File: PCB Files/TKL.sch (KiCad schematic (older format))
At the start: 632 parts, among them J1 USB_C, SW1 ESC, SW10 F9, SW100 RGUI_R2, SW101 RCTRL_R2, SW102 STEPPED_CAPS, SW103 RSHFT_175, SW104 Fn, SW105 BKSP_2U, SW11 F10, SW12 F11, SW13 F12, SW14 PRTSC, SW15 SCRLCK, SW16 PAUSE, SW17 GRV, SW18 1, SW19 2, SW2 F1, SW20 3, SW21 4, SW22 5, SW23 6, SW24 7, SW25 8, SW26 9, SW27 0, SW28 HIFEN, SW29 PLUS, SW3 F2, SW30 BCKSLSH, SW31 DEL, SW32 INS, SW33 HOME, SW34 PGUP, SW35 TAB, SW36 Q, SW37 W, SW38 E, SW39 R, SW4 F3, SW40 T, SW41 Y, SW42 U, SW43 I, SW44 O, SW45 P, SW46 LBRACES, SW47 RBRACES, SW48 BKSP_150, SW49 DEL, SW5 F4, SW50 END, SW51 PGDN, SW52 CAPS, SW53 A, SW54 S, SW55 D, SW56 F, SW57 G, SW58 H, SW59 J, SW6 F5, SW60 K, SW61 L, SW62 :, SW63 QUOTE, SW64 ENTER, SW65 LSHFT, SW66 Z, SW67 X, SW68 C, SW69 V, SW7 F6, SW70 B, SW71 N, SW72 M, SW73 <,, SW74 .>, SW75 /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

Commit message: Routed RGB76
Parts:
- added D96: 1N4148, acheron_Components:D_SOD-123, symbol Device:D
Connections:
- net Col1: now also U200.27 (ADC10/T0/PD7); no longer U200.40 (ADC1/PF1)
- net Col16: now also U200.25 (ADC8/PD4); no longer U200.27 (ADC10/T0/PD7)
- net Col17: now also U200.22 (PD5/~CTS~/XCK1); no longer U200.26 (ADC9/T1/PD6)
- net Col18: now also U200.21 (PD3/TXD1/~INT3~); no longer U200.25 (ADC8/PD4)
- net Col7: now also U200.40 (ADC1/PF1); no longer U200.36 (ADC7/PF7)
- net Col8: now also U200.36 (ADC7/PF7)
- net L4: no longer SW96.2 (Row)
- net RGB_DIN: now also U200.26 (ADC9/T1/PD6)
- net Row6: now also D96.1 (K)
- net at U75.5 (DO): now also RD103.2; no longer RD76.2
- net at U76.5 (DO): now also RD104.2; no longer RD103.2
- net at U103.5 (DO): now also RD76.2; no longer RD104.2
- new net: D96.2 (A), SW96.2 (Row)
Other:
- moved on the sheet: C103, C76, L103, L76, R103, R76, RD103, RD76, U103, U76

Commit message: Added last row RGB components to schematic
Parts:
- added C? (x14): 100nF, Capacitor_SMD:C_0805_2012Metric, symbol Device:C_Small
- added D93: 1N4148, acheron_Components:D_SOD-123, symbol Device:D
- added L? (x14): LED_BGRA, acheron_Components:LED_RGB_SMD_6028_2.8x3.5mm_Round, symbol Device:LED_BGRA
- added R? (x14): 100R, Resistor_SMD:R_0805_2012Metric, symbol Device:R_Small
- added RD? (x14): 33R, Resistor_SMD:R_0805_2012Metric, symbol Device:R_Small
- added U? (x14): WS2811M, acheron_Components:MSOP-8-1EP_3x3mm_P0.65mm_EP1.68x1.88mm, symbol acheronSymbols:WS2811M
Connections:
- net 5V: now also L?.4 (A), L?.4 (A), L?.4 (A), L?.4 (A), L?.4 (A), L?.4 (A), L?.4 (A), L?.4 (A), L?.4 (A), L?.4 (A), L?.4 (A), L?.4 (A), L?.4 (A), L?.4 (A), R?.1, R?.1, R?.1, R?.1, R?.1, R?.1, R?.1, R?.1, R?.1, R?.1, R?.1, R?.1, R?.1, R?.1
- net GND: now also C?.2, C?.2, C?.2, C?.2, C?.2, C?.2, C?.2, C?.2, C?.2, C?.2, C?.2, C?.2, C?.2, C?.2, U?.4 (GND), U?.4 (GND), U?.4 (GND), U?.4 (GND), U?.4 (GND), U?.4 (GND), U?.4 (GND), U?.4 (GND), U?.4 (GND), U?.4 (GND), U?.4 (GND), U?.4 (GND), U?.4 (GND), U?.4 (GND), U?.9 (GND), U?.9 (GND), U?.9 (GND), U?.9 (GND), U?.9 (GND), U?.9 (GND), U?.9 (GND), U?.9 (GND), U?.9 (GND), U?.9 (GND), U?.9 (GND), U?.9 (GND), U?.9 (GND), U?.9 (GND)
- net L3: no longer SW93.2 (Row)
- net Row5: now also D73.1 (K)
- net Row6: now also D93.1 (K)
- net at U77.5 (DO): now also RD?.2
- new net: D93.2 (A), SW93.2 (Row)
- new net: L?.3 (RK), U?.1 (OUTR) (x14)
- new net: L?.2 (GK), U?.2 (OUTG) (x14)
- new net: L?.1 (BK), U?.3 (OUTB) (x14)
- new net: RD?.2, U?.5 (DO) (x12)
- new net: RD?.1, U?.6 (DIN) (x13)
- new net: C?.1, R?.2, U?.8 (VDD) (x14)
- new net: RD?.1, U?.5 (DO)
- new net: RD?.2, U?.6 (DIN)
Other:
- moved on the sheet: D73, SW73

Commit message: Routed SW88 RGB LED
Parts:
- removed C? (x3): 100nF, Capacitor_SMD:C_0805_2012Metric, symbol Device:C_Small
- removed L? (x3): LED_BGRA, acheron_Components:LED_RGB_SMD_6028_2.8x3.5mm_Round, symbol Device:LED_BGRA
- removed R? (x3): 100R, Resistor_SMD:R_0805_2012Metric, symbol Device:R_Small
- removed RD? (x3): 33R, Resistor_SMD:R_0805_2012Metric, symbol Device:R_Small
- removed U? (x3): WS2811M, acheron_Components:MSOP-8-1EP_3x3mm_P0.65mm_EP1.68x1.88mm, symbol acheronSymbols:WS2811M
- gave numbers to parts that had none: 55
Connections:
- net at U77.5 (DO): now also RD88.2
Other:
- moved on the sheet: C78, C79, C80, C81, C82, C83, C84, C85, C86, C87, C88, L78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

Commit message: Placed last row LEDs
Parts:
- added C97, C99: 100nF, Capacitor_SMD:C_0805_2012Metric, symbol Device:C_Small
- added L91, L93, L94, L95, L96, L97, L99: LED_BGRA, acheron_Components:LED_RGB_SMD_6028_2.8x3.5mm_Round, symbol Device:LED_BGRA
- added R97, R99: 100R, Resistor_SMD:R_0805_2012Metric, symbol Device:R_Small
- added RD97, RD99: 33R, Resistor_SMD:R_0805_2012Metric, symbol Device:R_Small
- added U97, U99: WS2811M, acheron_Components:MSOP-8-1EP_3x3mm_P0.65mm_EP1.68x1.88mm, symbol acheronSymbols:WS2811M
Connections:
- net 5V: now also L97.4 (A), L99.4 (A), R97.1, R99.1
- net GND: now also C97.2, C99.2, U97.4 (GND), U97.9 (GND), U99.4 (GND), U99.9 (GND)
- net at RD82.2: now also U97.5 (DO); no longer U83.5 (DO)
- net at RD83.2: now also U99.5 (DO); no longer U84.5 (DO)
- new net: RD99.2, U84.5 (DO)
- new net: RD99.1, U99.6 (DIN)
- new net: L99.3 (RK), U99.1 (OUTR)
- new net: L99.2 (GK), U99.2 (OUTG)
- new net: L99.1 (BK), U99.3 (OUTB)
- new net: C99.1, R99.2, U99.8 (VDD)
- new net: RD97.1, U97.6 (DIN)
- new net: L97.3 (RK), U97.1 (OUTR)
- new net: L97.2 (GK), U97.2 (OUTG)
- new net: L97.1 (BK), U97.3 (OUTB)
- new net: C97.1, R97.2, U97.8 (VDD)
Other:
- moved on the sheet: C78, C79, C80, C81, C82, C83, C84, L78, L79, L80, L81, L82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

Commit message: Update: routed more RGBs, removed split bottom row
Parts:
- removed C97, C99: 100nF, Capacitor_SMD:C_0805_2012Metric, symbol Device:C_Small
- removed D89, D96: 1N4148, acheron_Components:D_SOD-123, symbol Device:D
- removed L91, L94, L96, L97, L99: LED_BGRA, acheron_Components:LED_RGB_SMD_6028_2.8x3.5mm_Round, symbol Device:LED_BGRA
- removed R97, R99: 100R, Resistor_SMD:R_0805_2012Metric, symbol Device:R_Small
- removed RD97, RD99: 33R, Resistor_SMD:R_0805_2012Metric, symbol Device:R_Small
- removed SW91: LALT_B3, acheron_MX:MX100, symbol acheronSymbols:MXSwitch
- removed SW94: LSPC_R3, acheron_MX:MX225R, symbol acheronSymbols:MXSwitch
- removed SW96: RSPC_B3, acheron_MX:MX275R, symbol acheronSymbols:MXSwitch
- removed SW97: RGUI_R3, acheron_MX:MX125, symbol acheronSymbols:MXSwitch
- removed SW99: RALT_R3, acheron_MX:MX100, symbol acheronSymbols:MXSwitch
- removed U97, U99: WS2811M, acheron_Components:MSOP-8-1EP_3x3mm_P0.65mm_EP1.68x1.88mm, symbol acheronSymbols:WS2811M
- added C95: 100nF, Capacitor_SMD:C_0805_2012Metric, symbol Device:C_Small
- added R95: 100R, Resistor_SMD:R_0805_2012Metric, symbol Device:R_Small
- added RD95: 33R, Resistor_SMD:R_0805_2012Metric, symbol Device:R_Small
- added U95: WS2811M, acheron_Components:MSOP-8-1EP_3x3mm_P0.65mm_EP1.68x1.88mm, symbol acheronSymbols:WS2811M
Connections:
- net 5V: now also L95.4 (A), R95.1
- net GND: now also C95.2, U95.4 (GND), U95.9 (GND)
- net at RD82.2: now also U95.5 (DO)
- net at RD83.2: now also U84.5 (DO)
- net at U83.5 (DO): now also RD95.2
- net at L95.1 (BK): now also U95.3 (OUTB)
- net at L95.2 (GK): now also U95.2 (OUTG)
- net at L95.3 (RK): now also U95.1 (OUTR)
- new net: RD95.1, U95.6 (DIN)
- new net: C95.1, R95.2, U95.8 (VDD)
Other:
- moved on the sheet: L95

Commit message: Update: Finish routing
- All tracks were routed

- There are some extra pins that need to be broken out.

- Also the serial programming ISP pins need to be broken out.

- After that is done, run DRC and correct eventual flaws
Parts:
- removed RD17: 33R, Resistor_SMD:R_0805_2012Metric, symbol Device:R_Small
- added C93: 100nF, Capacitor_SMD:C_0805_2012Metric, symbol Device:C_Small
- added R93: 100R, Resistor_SMD:R_0805_2012Metric, symbol Device:R_Small
- added RD93: 33R, Resistor_SMD:R_0805_2012Metric, symbol Device:R_Small
- added U93: WS2811M, acheron_Components:MSOP-8-1EP_3x3mm_P0.65mm_EP1.68x1.88mm, symbol acheronSymbols:WS2811M
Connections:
- net 5V: now also L93.4 (A), R93.1
- net GND: now also C93.2, U93.4 (GND), U93.9 (GND)
- net at RD95.2: now also U82.5 (DO); no longer U83.5 (DO)
- net at U95.5 (DO): now also RD81.2; no longer RD82.2
- net at U81.5 (DO): now also RD93.2; no longer RD80.2
- net at L93.1 (BK): now also U93.3 (OUTB)
- net at L93.2 (GK): now also U93.2 (OUTG)
- net at L93.3 (RK): now also U93.1 (OUTR)
- new net: RD93.1, U93.6 (DIN)
- new net: RD80.2, U93.5 (DO)
- new net: C93.1, R93.2, U93.8 (VDD)
- new net: RD82.2, U83.5 (DO)
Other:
- moved on the sheet: C78, C79, C80, C82, C95, L78, L79, L80, L82, L93, L95, R78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

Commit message: Run DRC, solve issues
- DRC was run and some issues arose. This means that some tracks needed
to be re-routed.

- Almost all columns and rows routed, except for Col12, Col15 and Row6.

- The ISP JTAG pins were broken out

- Some silkscreens were re-done for clarification

- The shield copper fill was further distanced from the GND copper fill

- A switch that did not correspond to any layout was removed

- The D+/D- USB differential pair now has a 20mil clearance
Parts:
- removed C93: 100nF, Capacitor_SMD:C_0805_2012Metric, symbol Device:C_Small
- removed D93: 1N4148, acheron_Components:D_SOD-123, symbol Device:D
- removed L93: LED_BGRA, acheron_Components:LED_RGB_SMD_6028_2.8x3.5mm_Round, symbol Device:LED_BGRA
- removed R93: 100R, Resistor_SMD:R_0805_2012Metric, symbol Device:R_Small
- removed RD93: 33R, Resistor_SMD:R_0805_2012Metric, symbol Device:R_Small
- removed SW93: LGUI_B3, acheron_MX:MX125, symbol acheronSymbols:MXSwitch
- removed U93: WS2811M, acheron_Components:MSOP-8-1EP_3x3mm_P0.65mm_EP1.68x1.88mm, symbol acheronSymbols:WS2811M
- added J2: AVR-ISP-6, acheron_Connectors:PinHeader_2x3_P2.54mm_Vertical, symbol Connector:AVR-ISP-6
- X1: footprint Crystal:Crystal_SMD_2016-4Pin_2.0x1.6mm -> acheron_Components:Crystal_SMD_2016-4Pin_2.0x1.6mm
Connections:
- net 5V: now also J2.2 (VCC)
- net Col14: now also J2.1 (MISO)
- net Col9: now also U200.20 (PD2/RDX1/~INT2~)
- net GND: now also J2.6 (GND)
- net Row3: now also J2.3 (SCK)
- net Row5: now also U200.19 (PD1/SDA/~INT1~)
- net at U81.5 (DO): now also RD80.2
- net RST renamed ~RST
- net ~RST: now also J2.5 (~RST)
- net Row2 renamed MOSI
- net MOSI: now also J2.4 (MOSI)
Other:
- note added: "ISP"
- moved on the sheet: G1, G2, G3

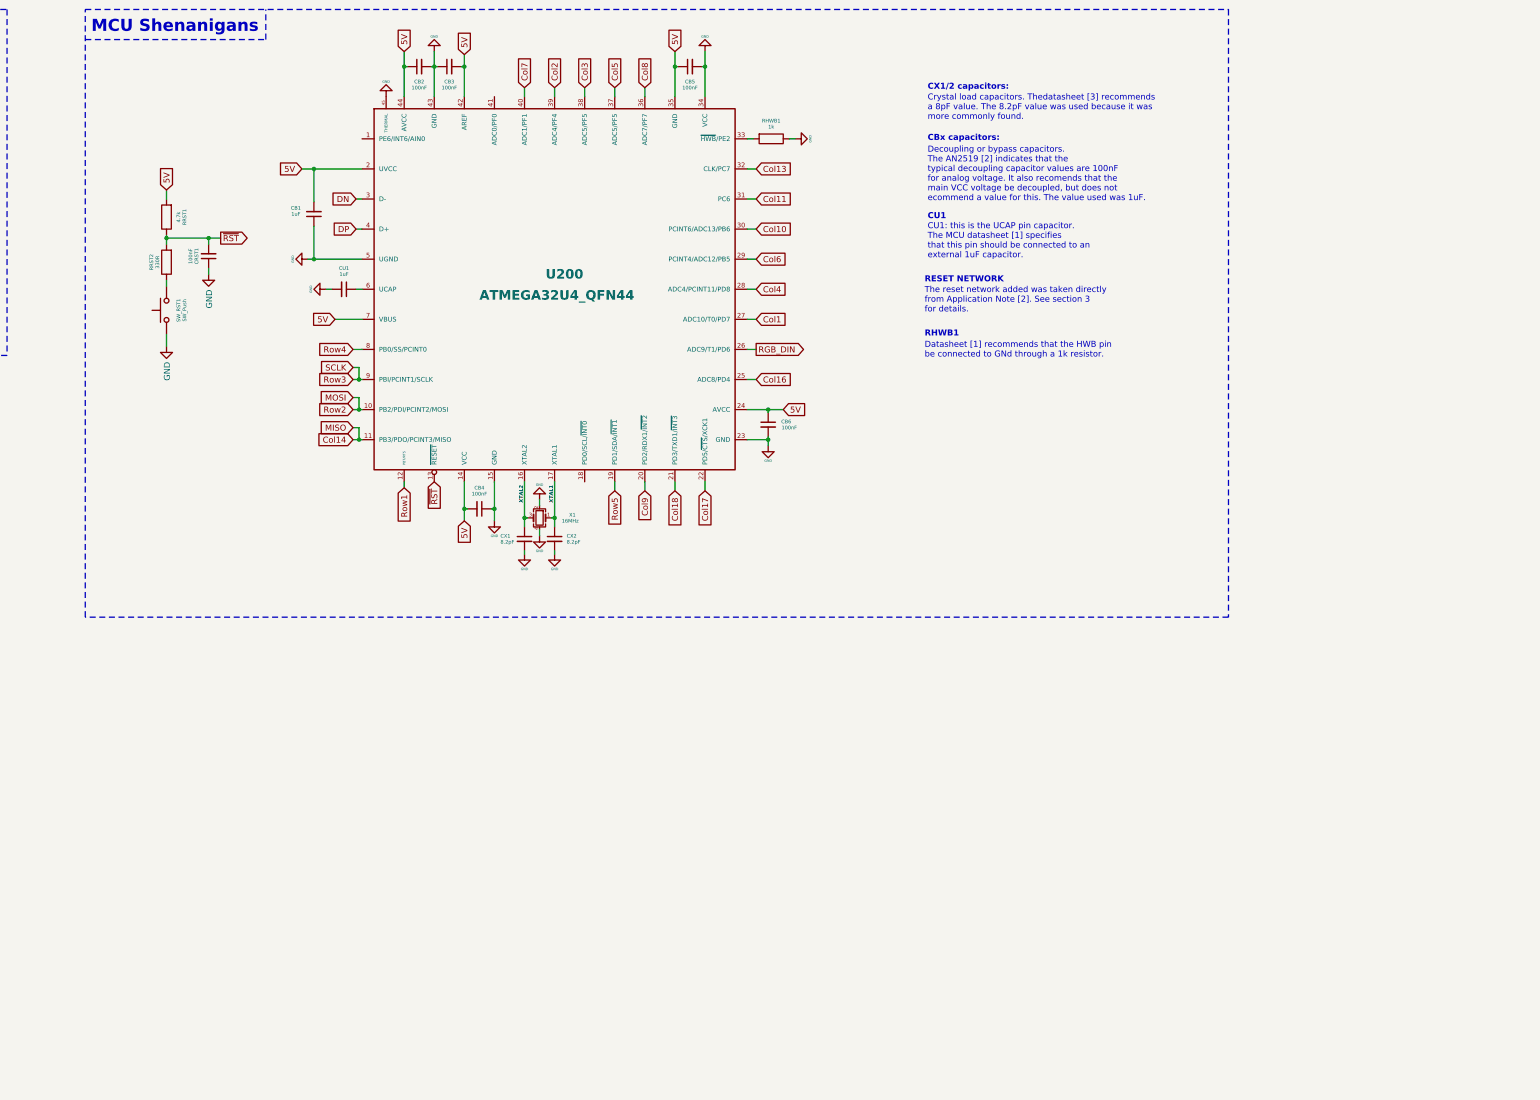
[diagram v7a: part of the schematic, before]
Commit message: Route rest of cols and rows
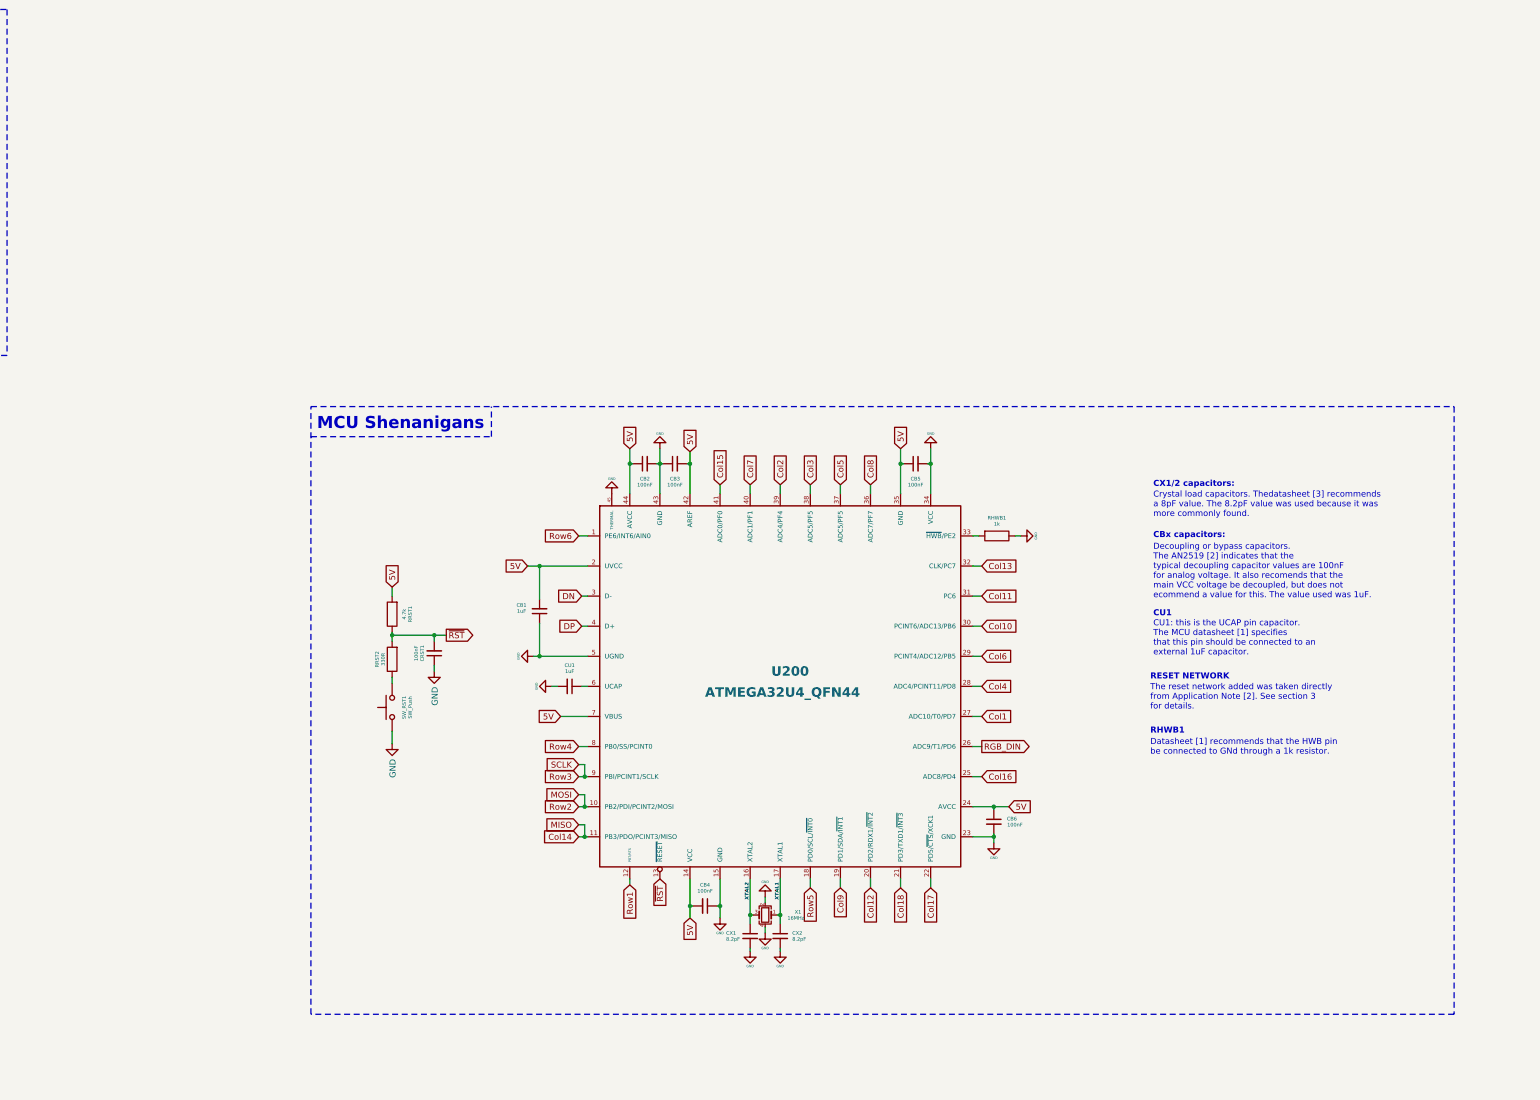
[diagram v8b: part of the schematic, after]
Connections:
- net Col12: now also U200.20 (PD2/RDX1/~INT2~)
- net Col15: now also U200.41 (ADC0/PF0)
- net Col9: now also U200.19 (PD1/SDA/~INT1~); no longer U200.20 (PD2/RDX1/~INT2~)
- net Row5: now also U200.18 (PD0/SCL/~INT0~); no longer U200.19 (PD1/SDA/~INT1~)
- net Row6: now also U200.1 (PE6/INT6/AIN0)
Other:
- moved on the sheet: CB1, CB2, CB3, CB4, CB5, CB6, CRST1, CU1, CX1, CX2, RHWB1, RRST1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
